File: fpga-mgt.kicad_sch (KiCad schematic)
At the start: 11 parts, among them U4 XC7K160T-FFG676

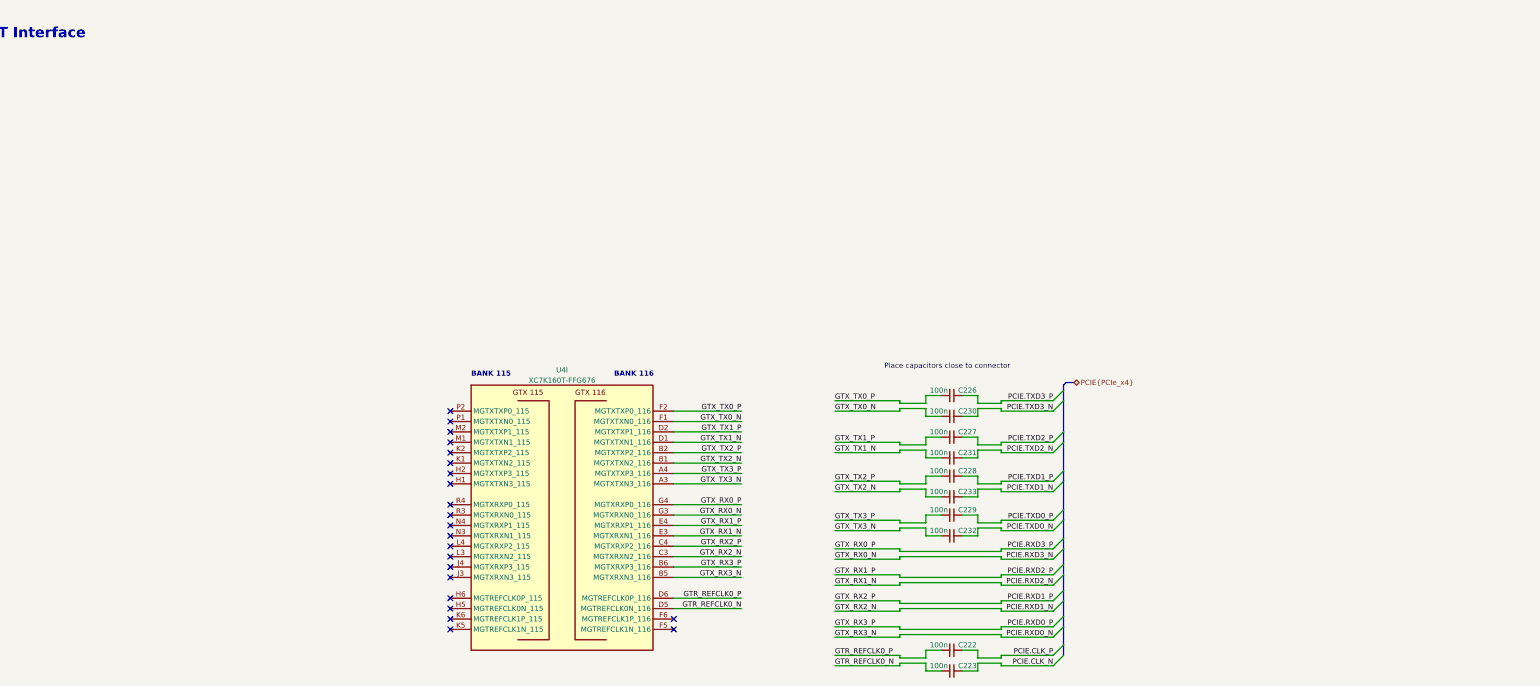
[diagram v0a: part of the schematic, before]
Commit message: [#66312] Reconnect PCIe to GTX 224
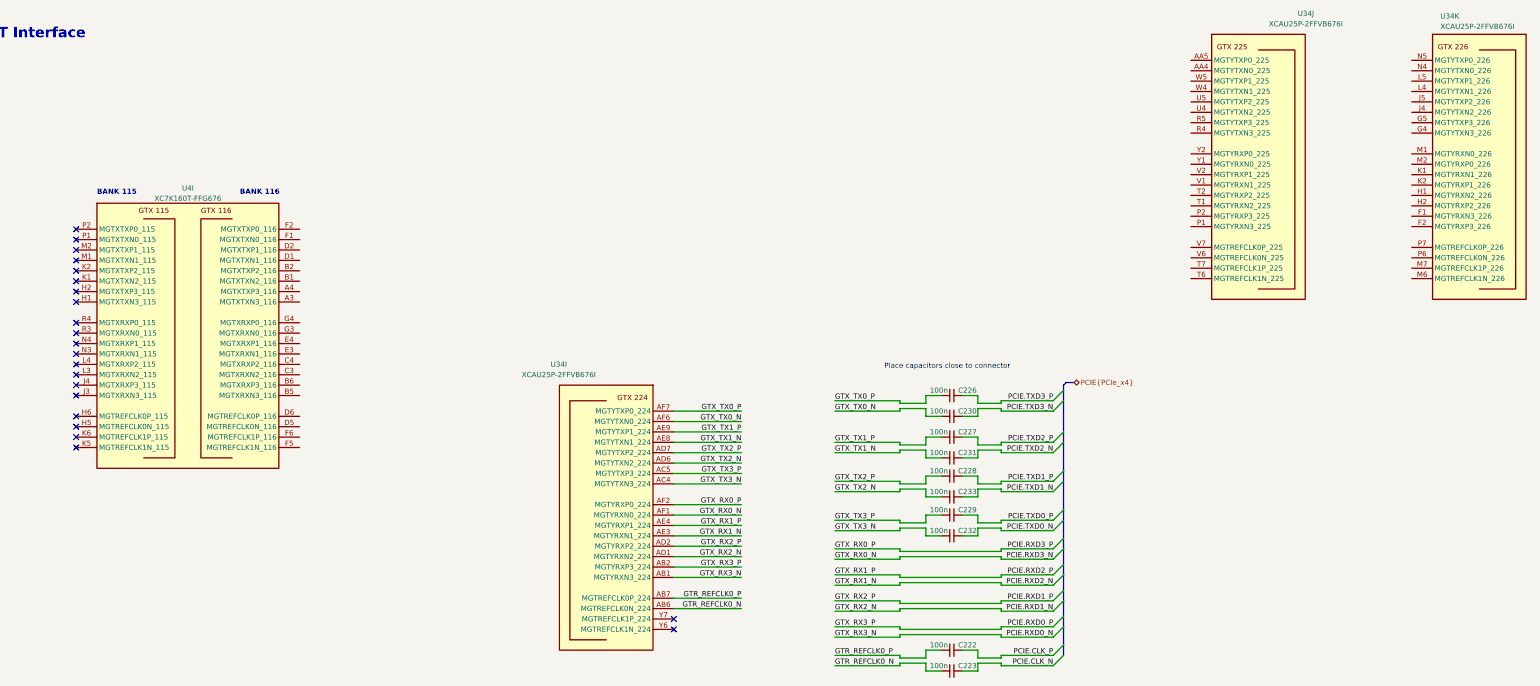
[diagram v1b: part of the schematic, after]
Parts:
- added U34: XCAU25P-2FFVB676I, antmicro-footprints:BGA-676_27x27mm_Layout26x26_P1x1mm_FFVB676, symbol antmicroFPGAChips:XCAU25P-2FFVB676I
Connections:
- net GTR_REFCLK0_N: now also U34.AB6 (MGTREFCLK0N_224); no longer U4.D5 (MGTREFCLK0N_116)
- net GTR_REFCLK0_P: now also U34.AB7 (MGTREFCLK0P_224); no longer U4.D6 (MGTREFCLK0P_116)
- net GTX_RX0_N: now also U34.AF1 (MGTYRXN0_224); no longer U4.G3 (MGTXRXN0_116)
- net GTX_RX0_P: now also U34.AF2 (MGTYRXP0_224); no longer U4.G4 (MGTXRXP0_116)
- net GTX_RX1_N: now also U34.AE3 (MGTYRXN1_224); no longer U4.E3 (MGTXRXN1_116)
- net GTX_RX1_P: now also U34.AE4 (MGTYRXP1_224); no longer U4.E4 (MGTXRXP1_116)
- net GTX_RX2_N: now also U34.AD1 (MGTYRXN2_224); no longer U4.C3 (MGTXRXN2_116)
- net GTX_RX2_P: now also U34.AD2 (MGTYRXP2_224); no longer U4.C4 (MGTXRXP2_116)
- net GTX_RX3_N: now also U34.AB1 (MGTYRXN3_224); no longer U4.B5 (MGTXRXN3_116)
- net GTX_RX3_P: now also U34.AB2 (MGTYRXP3_224); no longer U4.B6 (MGTXRXP3_116)
- net GTX_TX0_N: now also U34.AF6 (MGTYTXN0_224); no longer U4.F1 (MGTXTXN0_116)
- net GTX_TX0_P: now also U34.AF7 (MGTYTXP0_224); no longer U4.F2 (MGTXTXP0_116)
- net GTX_TX1_N: now also U34.AE8 (MGTYTXN1_224); no longer U4.D1 (MGTXTXN1_116)
- net GTX_TX1_P: now also U34.AE9 (MGTYTXP1_224); no longer U4.D2 (MGTXTXP1_116)
- net GTX_TX2_N: now also U34.AD6 (MGTYTXN2_224); no longer U4.B1 (MGTXTXN2_116)
- net GTX_TX2_P: now also U34.AD7 (MGTYTXP2_224); no longer U4.B2 (MGTXTXP2_116)
- net GTX_TX3_N: now also U34.AC4 (MGTYTXN3_224); no longer U4.A3 (MGTXTXN3_116)
- net GTX_TX3_P: now also U34.AC5 (MGTYTXP3_224); no longer U4.A4 (MGTXTXP3_116)
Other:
- moved on the sheet: U4I

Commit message: [#65754] Rename project
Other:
- title: SO-DIMM DDR5 Tester -> RDIMM DDR5 Tester
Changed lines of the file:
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@@
   (paper "A3")
   (title_block
-    (title "SO-DIMM DDR5 Tester")
-    (date "2024-04-23")
-    (rev "1.2.0")
+    (title "RDIMM DDR5 Tester")
+    (date "2024-09-26")
+    (rev "2.0.0")
     (comment 1 "www.antmicro.com")
     (comment 2 "Antmicro Ltd")
@@
     (pin "2")
     (instances
-      (project "rdimm-ddr5-tester-ultrascale-plus"
+      (project "data-center-rdimm-ddr5-tester"
         (path "/1faa6543-e26a-4449-8bac-ee14b9f19e5f/e98c799f-d02e-47b6-ad5c-871bd722b830"
           (reference "C227") (unit 1)
@@
     (pin "AD11")
     (instances
-      (project "rdimm-ddr5-tester-ultrascale-plus"
+      (project "data-center-rdimm-ddr5-tester"
         (path "/1faa6543-e26a-4449-8bac-ee14b9f19e5f/e98c799f-d02e-47b6-ad5c-871bd722b830"
           (reference "U34") (unit 11)
@@
     (pin "AD11")
     (instances
-      (project "rdimm-ddr5-tester-ultrascale-plus"
+      (project "data-center-rdimm-ddr5-tester"
         (path "/1faa6543-e26a-4449-8bac-ee14b9f19e5f/e98c799f-d02e-47b6-ad5c-871bd722b830"
           (reference "U34") (unit 9)
@@
     (pin "2")
     (instances
-      (project "rdimm-ddr5-tester-ultrascale-plus"
+      (project "data-center-rdimm-ddr5-tester"
         (path "/1faa6543-e26a-4449-8bac-ee14b9f19e5f/e98c799f-d02e-47b6-ad5c-871bd722b830"
           (reference "C222") (unit 1)
@@
     (pin "2")
     (instances
-      (project "rdimm-ddr5-tester-ultrascale-plus"
+      (project "data-center-rdimm-ddr5-tester"
         (path "/1faa6543-e26a-4449-8bac-ee14b9f19e5f/e98c799f-d02e-47b6-ad5c-871bd722b830"
           (reference "C228") (unit 1)
@@
     (pin "2")
     (instances
-      (project "rdimm-ddr5-tester-ultrascale-plus"
+      (project "data-center-rdimm-ddr5-tester"
         (path "/1faa6543-e26a-4449-8bac-ee14b9f19e5f/e98c799f-d02e-47b6-ad5c-871bd722b830"
           (reference "C232") (unit 1)
@@
     (pin "2")
     (instances
-      (project "rdimm-ddr5-tester-ultrascale-plus"
+      (project "data-center-rdimm-ddr5-tester"
         (path "/1faa6543-e26a-4449-8bac-ee14b9f19e5f/e98c799f-d02e-47b6-ad5c-871bd722b830"
           (reference "C226") (unit 1)
@@
     (pin "2")
     (instances
-      (project "rdimm-ddr5-tester-ultrascale-plus"
+      (project "data-center-rdimm-ddr5-tester"
         (path "/1faa6543-e26a-4449-8bac-ee14b9f19e5f/e98c799f-d02e-47b6-ad5c-871bd722b830"
           (reference "C230") (unit 1)
@@
     (pin "2")
     (instances
-      (project "rdimm-ddr5-tester-ultrascale-plus"
+      (project "data-center-rdimm-ddr5-tester"
         (path "/1faa6543-e26a-4449-8bac-ee14b9f19e5f/e98c799f-d02e-47b6-ad5c-871bd722b830"
           (reference "C233") (unit 1)
@@
     (pin "T6")
     (instances
-      (project "rdimm-ddr5-tester-ultrascale-plus"
+      (project "data-center-rdimm-ddr5-tester"
         (path "/1faa6543-e26a-4449-8bac-ee14b9f19e5f/e98c799f-d02e-47b6-ad5c-871bd722b830"
           (reference "U4") (unit 9)
@@
     (pin "AD11")
     (instances
-      (project "rdimm-ddr5-tester-ultrascale-plus"
+      (project "data-center-rdimm-ddr5-tester"
         (path "/1faa6543-e26a-4449-8bac-ee14b9f19e5f/e98c799f-d02e-47b6-ad5c-871bd722b830"
           (reference "U34") (unit 10)
@@
     (pin "2")
     (instances
-      (project "rdimm-ddr5-tester-ultrascale-plus"
+      (project "data-center-rdimm-ddr5-tester"
         (path "/1faa6543-e26a-4449-8bac-ee14b9f19e5f/e98c799f-d02e-47b6-ad5c-871bd722b830"
           (reference "C229") (unit 1)
@@
     (pin "2")
     (instances
-      (project "rdimm-ddr5-tester-ultrascale-plus"
+      (project "data-center-rdimm-ddr5-tester"
         (path "/1faa6543-e26a-4449-8bac-ee14b9f19e5f/e98c799f-d02e-47b6-ad5c-871bd722b830"
           (reference "C223") (unit 1)
@@
     (pin "2")
     (instances
-      (project "rdimm-ddr5-tester-ultrascale-plus"
+      (project "data-center-rdimm-ddr5-tester"
         (path "/1faa6543-e26a-4449-8bac-ee14b9f19e5f/e98c799f-d02e-47b6-ad5c-871bd722b830"
           (reference "C231") (unit 1)

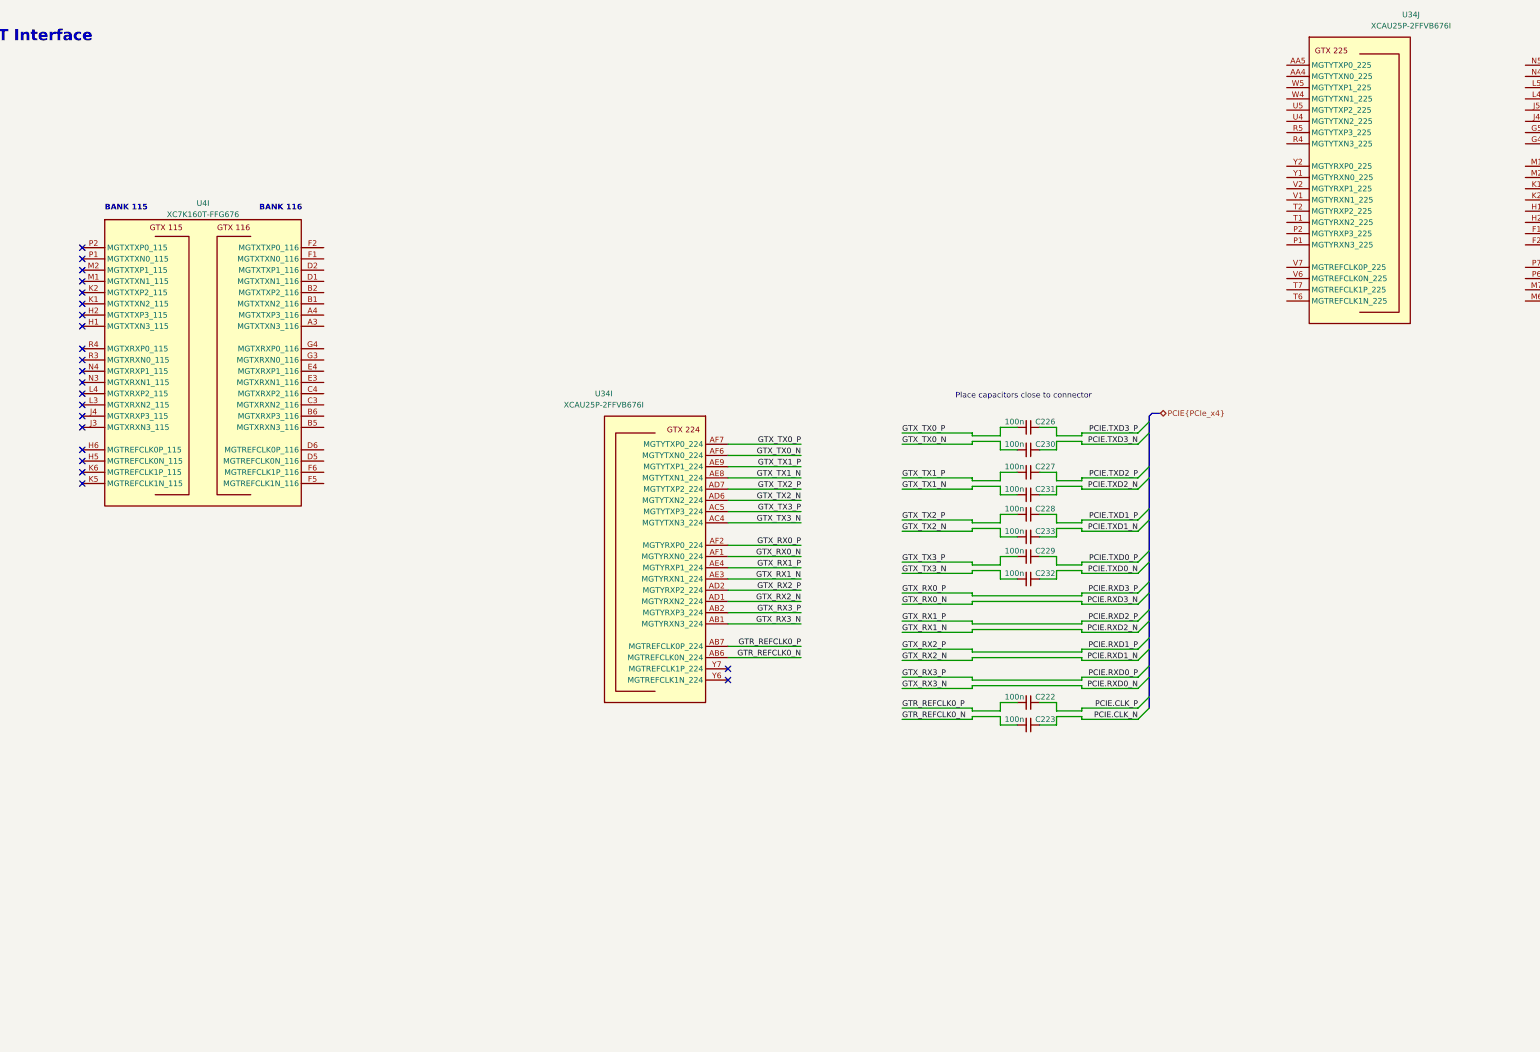
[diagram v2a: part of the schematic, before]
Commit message: [#66312] Reconnect GTY 224 and 225 for x8 PCIe configuration
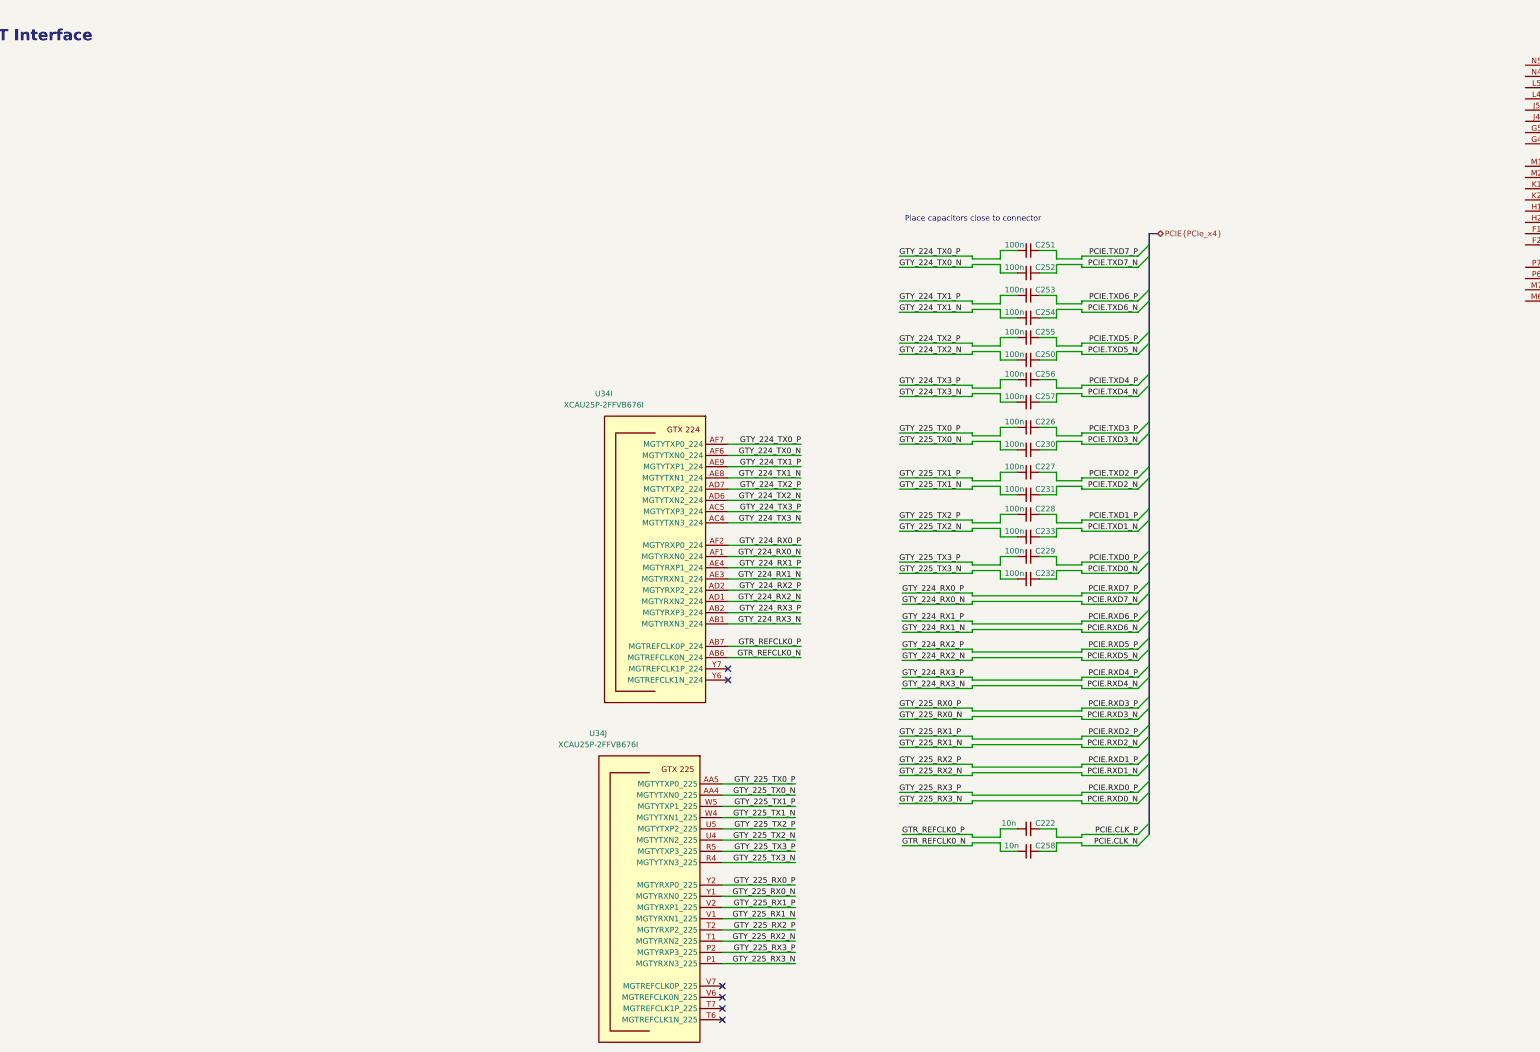
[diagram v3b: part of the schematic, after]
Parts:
- removed C222, C223: C_100n_0402, antmicro-footprints:C_0402_1005Metric, symbol antmicroCapacitors0402:C_100n_0402
- removed U4: XC7K160T-FFG676, antmicro-footprints:BGA-676_27x27mm_Layout26x26_P1x1mm_FFG676, symbol antmicroFPGAChips:XC7K160T-FFG676
- added C222, C258: C_10n_0402, antmicro-footprints:C_0402_1005Metric, symbol antmicroCapacitors0402:C_10n_0402
- added C250, C251, C252, C253, C254, C255, C256, C257: C_100n_0402, antmicro-footprints:C_0402_1005Metric, symbol antmicroCapacitors0402:C_100n_0402
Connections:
- net GTR_REFCLK0_N: now also C222.1
- net GTR_REFCLK0_P: now also C258.1
- net PCIE.CLK_N: now also C222.2
- net PCIE.CLK_P: now also C258.2
- net GTY_225_TX0_N: now reaches U34.AA4 (MGTYTXN0_225)
- net GTY_225_TX0_N: now also C230.2
- net GTY_225_TX0_P: now reaches U34.AA5 (MGTYTXP0_225)
- net GTY_225_TX0_P: now also C226.2
- net GTY_225_RX3_N: now reaches U34.P1 (MGTYRXN3_225)
- net GTY_225_RX3_P: now reaches U34.P2 (MGTYRXP3_225)
- net GTY_225_TX3_N: now reaches U34.R4 (MGTYTXN3_225)
- net GTY_225_TX3_N: now also C232.2
- net GTY_225_TX3_P: now reaches U34.R5 (MGTYTXP3_225)
- net GTY_225_TX3_P: now also C229.2
- net GTY_225_RX2_N: now reaches U34.T1 (MGTYRXN2_225)
- net GTY_225_RX2_P: now reaches U34.T2 (MGTYRXP2_225)
- net GTY_225_TX2_N: now reaches U34.U4 (MGTYTXN2_225)
- net GTY_225_TX2_N: now also C233.1
- net GTY_225_TX2_P: now reaches U34.U5 (MGTYTXP2_225)
- net GTY_225_TX2_P: now also C228.2
- net GTY_225_RX1_N: now reaches U34.V1 (MGTYRXN1_225)
- net GTY_225_RX1_P: now reaches U34.V2 (MGTYRXP1_225)
- net GTY_225_TX1_N: now reaches U34.W4 (MGTYTXN1_225)
- net GTY_225_TX1_N: now also C231.2
- net GTY_225_TX1_P: now reaches U34.W5 (MGTYTXP1_225)
- net GTY_225_TX1_P: now also C227.2
- net GTY_225_RX0_N: now reaches U34.Y1 (MGTYRXN0_225)
- net GTY_225_RX0_P: now reaches U34.Y2 (MGTYRXP0_225)
- net GTX_RX0_N renamed GTY_224_RX0_N
- net GTX_RX0_P renamed GTY_224_RX0_P
- net GTX_RX1_N renamed GTY_224_RX1_N
- net GTX_RX1_P renamed GTY_224_RX1_P
- net GTX_RX2_N renamed GTY_224_RX2_N
- net GTX_RX2_P renamed GTY_224_RX2_P
- net GTX_RX3_N renamed GTY_224_RX3_N
- net GTX_RX3_P renamed GTY_224_RX3_P
- net GTX_TX0_N renamed GTY_224_TX0_N
- net GTY_224_TX0_N: now also C252.2; no longer C230.2
- net GTX_TX0_P renamed GTY_224_TX0_P
- net GTY_224_TX0_P: now also C251.2; no longer C226.2
- net GTX_TX1_N renamed GTY_224_TX1_N
- net GTY_224_TX1_N: now also C254.2; no longer C231.2
- net GTX_TX1_P renamed GTY_224_TX1_P
- net GTY_224_TX1_P: now also C253.2; no longer C227.2
- net GTX_TX2_N renamed GTY_224_TX2_N
- net GTY_224_TX2_N: now also C250.1; no longer C233.1
- net GTX_TX2_P renamed GTY_224_TX2_P
- net GTY_224_TX2_P: now also C255.2; no longer C228.2
- net GTX_TX3_N renamed GTY_224_TX3_N
- net GTY_224_TX3_N: now also C257.2; no longer C232.2
- net GTX_TX3_P renamed GTY_224_TX3_P
- net GTY_224_TX3_P: now also C256.2; no longer C229.2
- new net PCIE.TXD4_N: C257.1
- new net PCIE.TXD4_P: C256.1
- new net PCIE.TXD5_N: C250.2
- new net PCIE.TXD5_P: C255.1
- new net PCIE.TXD6_N: C254.1
- new net PCIE.TXD6_P: C253.1
- new net PCIE.TXD7_N: C252.1
- new net PCIE.TXD7_P: C251.1
- no-connect marks 22 -> 6
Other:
- note removed: "BANK 115"
- note removed: "BANK 116"
- moved on the sheet: U34J

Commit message: [#66312] Connect x8 PCIe
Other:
- moved on the sheet: C222, C226, C227, C228, C229, C230, C231, C232, C233, C250, C251, C252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
